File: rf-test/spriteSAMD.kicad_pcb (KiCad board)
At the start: 2 copper layers, 25.7 x 29.8 mm, 7 parts, among them J1 Conn_01x08_Female, J2 Conn_Coaxial, J3 Conn_01x08_Female, U1 RFM95W-915S2

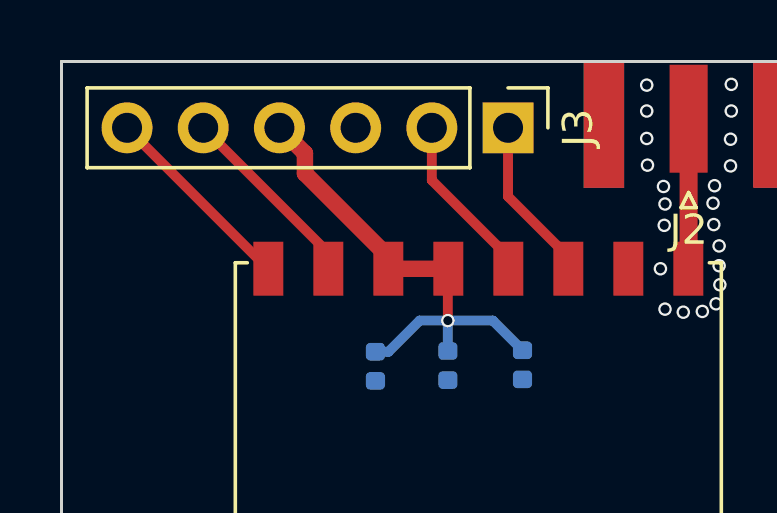
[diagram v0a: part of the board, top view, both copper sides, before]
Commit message: Fixed Mistake in RF Test Board
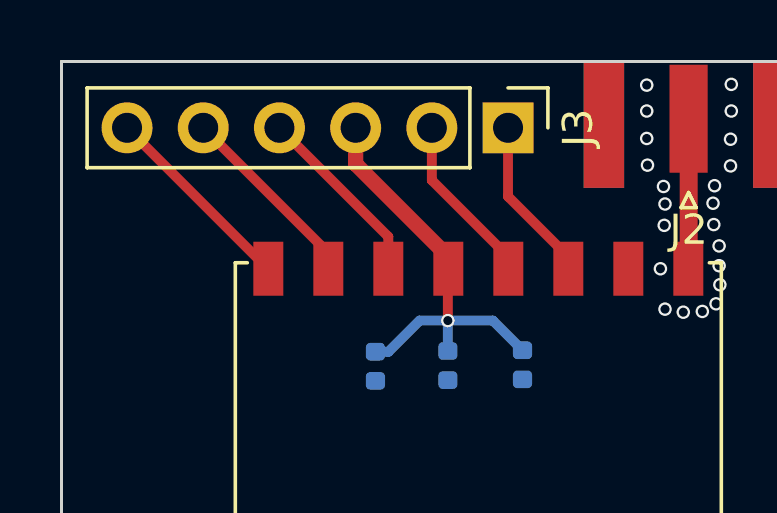
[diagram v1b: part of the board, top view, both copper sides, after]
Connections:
- C1 pad 1: RF_DIO0 -> +3V3
- C2 pad 1: RF_DIO0 -> +3V3
- C3 pad 1: RF_DIO0 -> +3V3
- J1 pad 1: (no net) -> Net-(J1-Pad1)
- J3 pad 3: (no net) -> +3V3
- U1 pad 13: RF_DIO0 -> +3V3
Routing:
- net +3V3: track 0.00 -> 14.5 mm, vias 0 -> 1
- net RF_DIO0: track 16.7 -> 6.20 mm, vias 1 -> 0
- net GND: vias 21 -> 22
- net (no net): vias 1 -> 0
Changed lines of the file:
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@@
     (zones 0)
     (modules 7)
-    (nets 14)
+    (nets 16)
   )
   (page A4)
@@
   )
   (setup
-    (last_trace_width 0.6)
+    (last_trace_width 0.508)
     (user_trace_width 0.0889)
     (user_trace_width 0.127)
@@
     (user_trace_width 1.27)
     (trace_clearance 0.127)
-    (zone_clearance 0.127)
+    (zone_clearance 0.2)
     (zone_45_only no)
     (trace_min 0.0889)
@@
   (net 12 P7)
   (net 13 "Net-(J2-Pad1)")
+  (net 14 +3V3)
+  (net 15 "Net-(J1-Pad1)")
   (net_class Default "This is the default net class."
     (clearance 0.127)
@@
     (uvia_dia 0.3)
     (uvia_drill 0.1)
+    (add_net +3V3)
     (add_net MISO)
     (add_net MOSI)
+    (add_net "Net-(J1-Pad1)")
     (add_net "Net-(J2-Pad1)")
     (add_net P7)
@@
     (pad 4 thru_hole oval (at 0 7.62 270) (size 1.7 1.7) (drill 1) (layers *.Cu *.Mask)
       (net 9 RF_DIO0))
-    (pad 3 thru_hole oval (at 0 5.08 270) (size 1.7 1.7) (drill 1) (layers *.Cu *.Mask))
+    (pad 3 thru_hole oval (at 0 5.08 270) (size 1.7 1.7) (drill 1) (layers *.Cu *.Mask)
+      (net 14 +3V3))
     (pad 2 thru_hole oval (at 0 2.54 270) (size 1.7 1.7) (drill 1) (layers *.Cu *.Mask)
       (net 8 RF_BUSY))
@@
       (net 1 GND))
     (pad 1 smd roundrect (at -0.485 0 270) (size 0.59 0.64) (layers Bottom B.Paste B.Mask) (roundrect_rratio 0.25)
-      (net 9 RF_DIO0))
+      (net 14 +3V3))
     (model ${KISYS3DMOD}/Capacitor_SMD.3dshapes/C_0402_1005Metric.wrl
       (at (xyz 0 0 0))
@@
       (net 1 GND))
     (pad 1 smd roundrect (at -0.485 0 270) (size 0.59 0.64) (layers Bottom B.Paste B.Mask) (roundrect_rratio 0.25)
-      (net 9 RF_DIO0))
+      (net 14 +3V3))
     (model ${KISYS3DMOD}/Capacitor_SMD.3dshapes/C_0402_1005Metric.wrl
       (at (xyz 0 0 0))
@@
       (net 1 GND))
     (pad 1 smd roundrect (at -0.485 0 270) (size 0.59 0.64) (layers Bottom B.Paste B.Mask) (roundrect_rratio 0.25)
-      (net 9 RF_DIO0))
+      (net 14 +3V3))
     (model ${KISYS3DMOD}/Capacitor_SMD.3dshapes/C_0402_1005Metric.wrl
       (at (xyz 0 0 0))
@@
     (pad 2 thru_hole oval (at 0 2.54 90) (size 1.7 1.7) (drill 1) (layers *.Cu *.Mask)
       (net 2 MISO))
-    (pad 1 thru_hole rect (at 0 0 90) (size 1.7 1.7) (drill 1) (layers *.Cu *.Mask))
+    (pad 1 thru_hole rect (at 0 0 90) (size 1.7 1.7) (drill 1) (layers *.Cu *.Mask)
+      (net 15 "Net-(J1-Pad1)"))
     (model ${KISYS3DMOD}/Connector_PinHeader_2.54mm.3dshapes/PinHeader_1x08_P2.54mm_Vertical.wrl
       (at (xyz 0 0 0))
@@
       (net 9 RF_DIO0))
     (pad 13 smd rect (at 7.9 -1 90) (size 1.8 1) (layers Top F.Paste F.Mask)
-      (net 9 RF_DIO0))
+      (net 14 +3V3))
     (pad 12 smd rect (at 7.9 1 90) (size 1.8 1) (layers Top F.Paste F.Mask)
       (net 8 RF_BUSY))
@@
   (gr_line (start 171.704 65.9384) (end 171.704 95.7072) (layer Edge.Cuts) (width 0.1))
   (gr_line (start 170.4086 65.9384) (end 171.704 65.9384) (layer Edge.Cuts) (width 0.1))
-  (via (at 168.3258 67.5894) (size 0.45) (drill 0.3) (layers Top Bottom) (net 0))
+  (via (at 168.3258 67.5894) (size 0.45) (drill 0.3) (layers Top Bottom) (net 1))
   (segment (start 166.893 91.709) (end 168.7322 93.5482) (width 0.3302) (layer Top) (net 1))
   (segment (start 166.893 88.6466) (end 166.893 91.709) (width 0.3302) (layer Top) (net 1))
@@
   (segment (start 160.893 72.8466) (end 160.893 72.4466) (width 0.3302) (layer Top) (net 8))
   (segment (start 160.893 72.4466) (end 158.3436 69.8972) (width 0.3302) (layer Top) (net 8))
-  (via (at 158.877 74.5744) (size 0.45) (drill 0.3) (layers Top Bottom) (net 9))
-  (segment (start 158.877 75.588) (end 158.877 74.5744) (width 0.3302) (layer Bottom) (net 9))
-  (segment (start 158.877 72.8626) (end 158.893 72.8466) (width 0.3302) (layer Top) (net 9))
-  (segment (start 158.877 74.5744) (end 158.877 72.8626) (width 0.3302) (layer Top) (net 9))
-  (segment (start 156.464 75.6134) (end 156.8982 75.6134) (width 0.3302) (layer Bottom) (net 9))
-  (segment (start 157.9372 74.5744) (end 158.877 74.5744) (width 0.3302) (layer Bottom) (net 9))
-  (segment (start 156.8982 75.6134) (end 157.9372 74.5744) (width 0.3302) (layer Bottom) (net 9))
-  (segment (start 160.378 74.5744) (end 158.877 74.5744) (width 0.3302) (layer Bottom) (net 9))
-  (segment (start 161.3662 75.5626) (end 160.378 74.5744) (width 0.3302) (layer Bottom) (net 9))
-  (segment (start 156.893 72.4466) (end 156.893 72.8466) (width 0.54864) (layer Top) (net 9))
-  (segment (start 154.113599 69.667199) (end 156.893 72.4466) (width 0.54864) (layer Top) (net 9))
-  (segment (start 153.2636 68.1482) (end 154.113599 68.998199) (width 0.54864) (layer Top) (net 9))
-  (segment (start 154.113599 68.998199) (end 154.113599 69.667199) (width 0.54864) (layer Top) (net 9))
-  (segment (start 156.893 72.8466) (end 158.893 72.8466) (width 0.54864) (layer Top) (net 9))
+  (segment (start 156.893 71.7776) (end 156.893 72.8466) (width 0.3302) (layer Top) (net 9))
+  (segment (start 153.2636 68.1482) (end 156.893 71.7776) (width 0.3302) (layer Top) (net 9))
+  (via (at 158.877 74.5744) (size 0.45) (drill 0.3) (layers Top Bottom) (net 14))
+  (segment (start 158.877 75.588) (end 158.877 74.5744) (width 0.3302) (layer Bottom) (net 14))
+  (segment (start 158.877 72.8626) (end 158.893 72.8466) (width 0.3302) (layer Top) (net 14))
+  (segment (start 158.877 74.5744) (end 158.877 72.8626) (width 0.3302) (layer Top) (net 14))
+  (segment (start 156.464 75.6134) (end 156.8982 75.6134) (width 0.3302) (layer Bottom) (net 14))
+  (segment (start 157.9372 74.5744) (end 158.877 74.5744) (width 0.3302) (layer Bottom) (net 14))
+  (segment (start 156.8982 75.6134) (end 157.9372 74.5744) (width 0.3302) (layer Bottom) (net 14))
+  (segment (start 160.378 74.5744) (end 158.877 74.5744) (width 0.3302) (layer Bottom) (net 14))
+  (segment (start 161.3662 75.5626) (end 160.378 74.5744) (width 0.3302) (layer Bottom) (net 14))
   (segment (start 154.893 72.3176) (end 154.893 72.8466) (width 0.3302) (layer Top) (net 10))
-  (segment (start 150.7236 68.1482) (end 154.893 72.3176) (width 0.3302) (layer Top) (net 10))
+  (segment (start 150.7198 68.1444) (end 154.8892 72.3138) (width 0.3302) (layer Top) (net 10))
   (segment (start 152.882 72.8466) (end 152.893 72.8466) (width 0.3302) (layer Top) (net 11))
   (segment (start 148.1836 68.1482) (end 152.882 72.8466) (width 0.3302) (layer Top) (net 11))
@@
   (segment (start 166.9034 72.8362) (end 166.893 72.8466) (width 0.6) (layer Top) (net 13))
   (segment (start 166.9034 67.8466) (end 166.9034 72.8362) (width 0.6) (layer Top) (net 13))
+  (segment (start 158.893 72.4466) (end 158.893 72.8466) (width 0.508) (layer Top) (net 14))
+  (segment (start 155.8036 69.3572) (end 158.893 72.4466) (width 0.508) (layer Top) (net 14))
+  (segment (start 155.8036 68.1482) (end 155.8036 69.3572) (width 0.508) (layer Top) (net 14))
   (zone (net 1) (net_name GND) (layer Top) (hatch edge 0.508)
     (connect_pads (clearance 0.127))
